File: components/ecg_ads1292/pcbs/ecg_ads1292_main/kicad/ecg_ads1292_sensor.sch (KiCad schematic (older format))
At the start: 36 parts, among them IC1 ADS1292IPBSR, U1 TPS73033DBVT

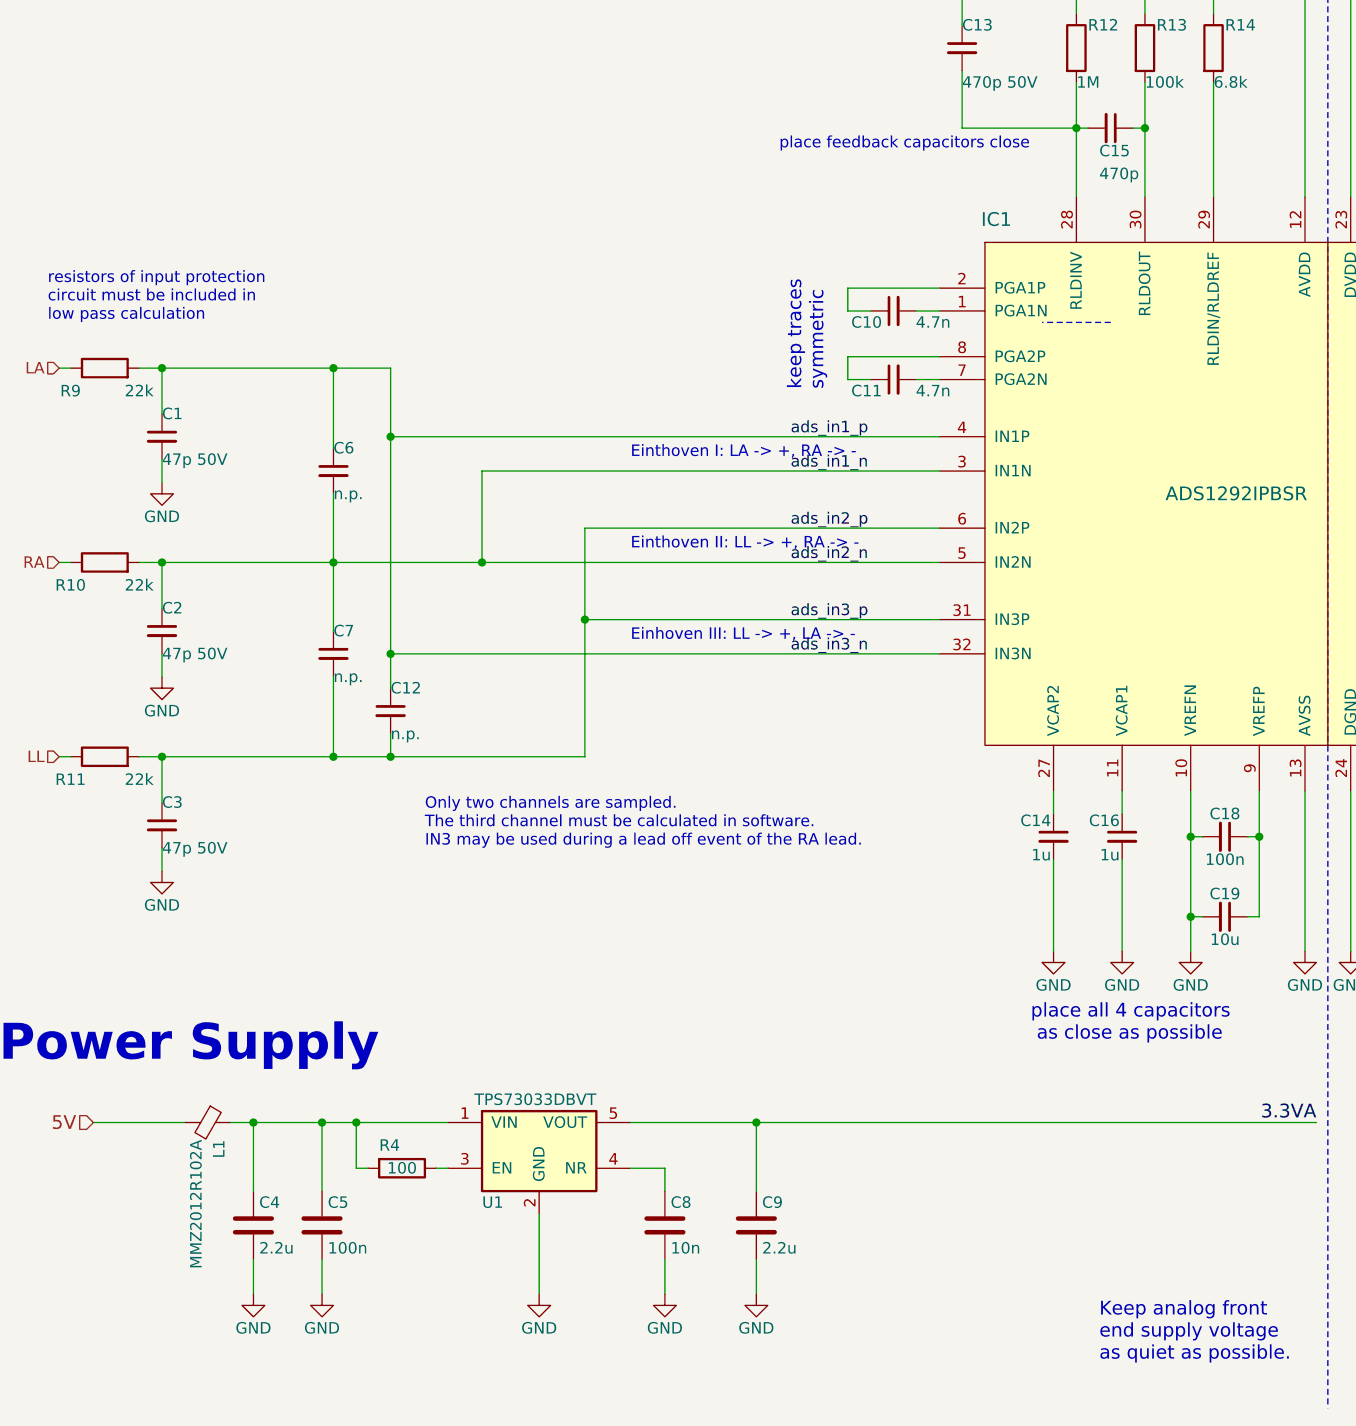
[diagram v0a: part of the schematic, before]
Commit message: update parts and add digikey PNs
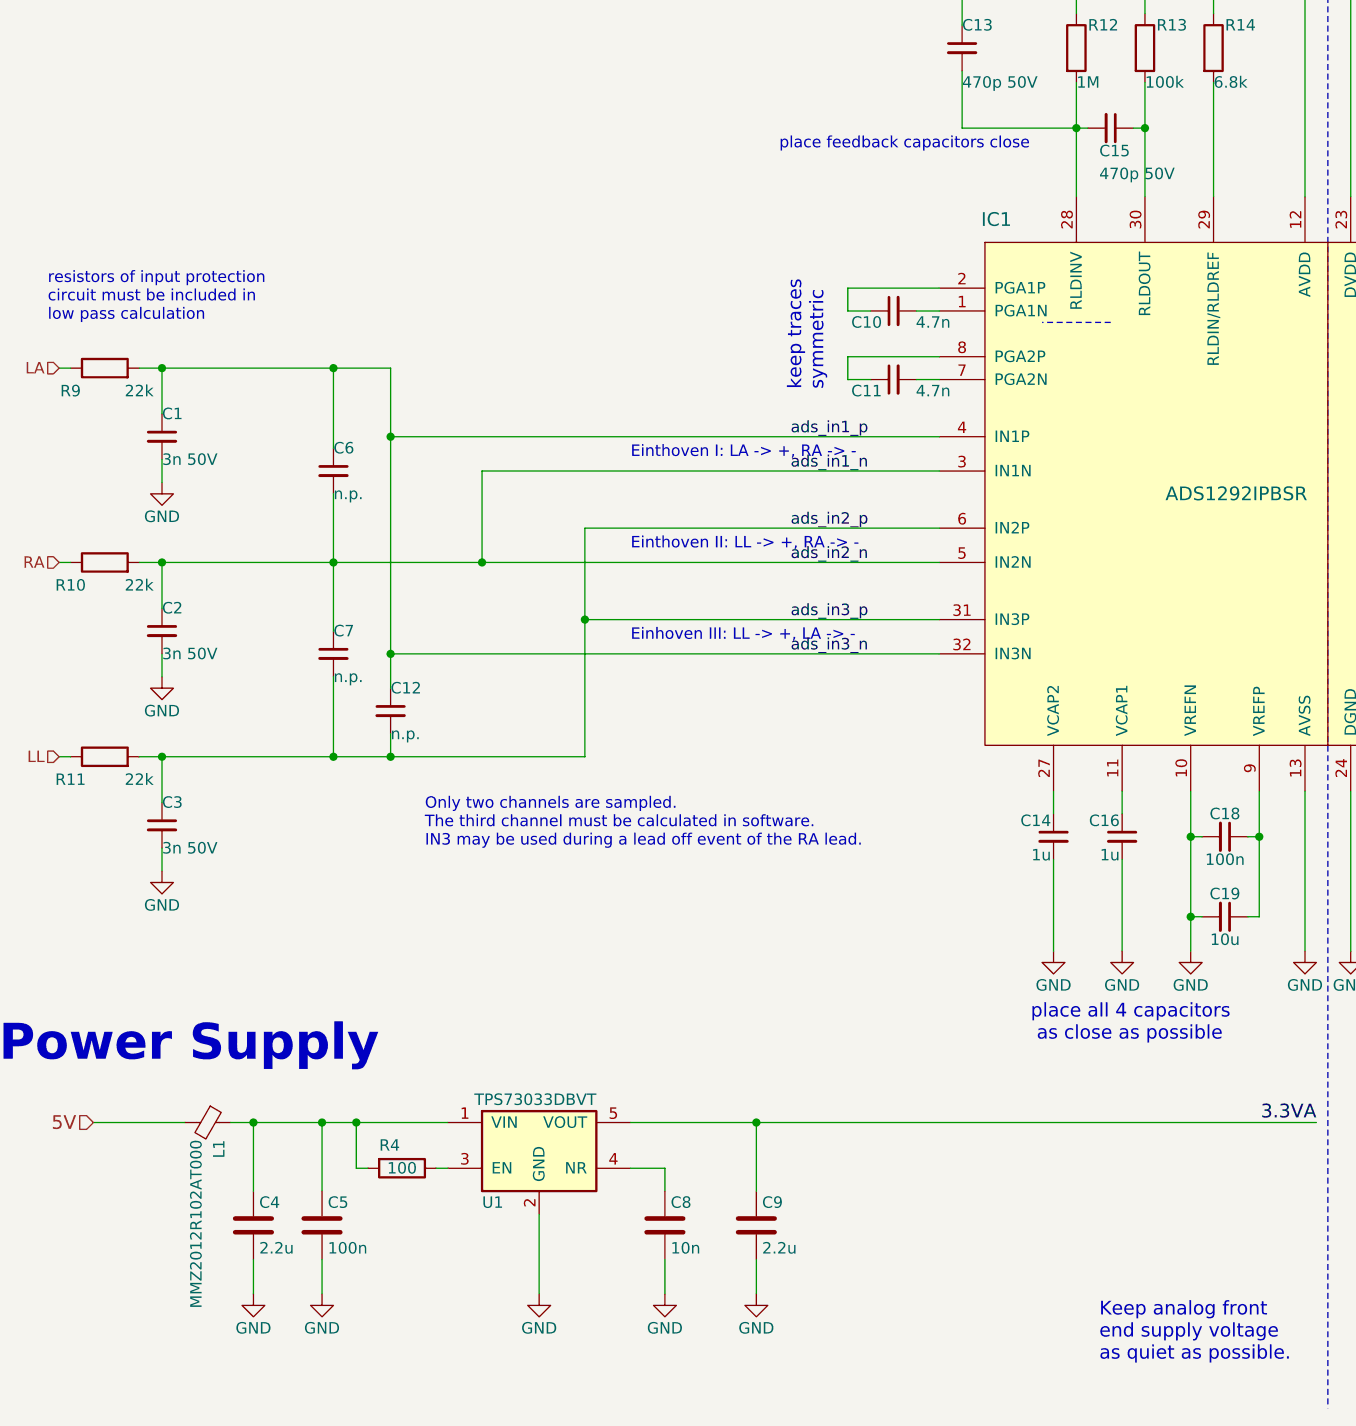
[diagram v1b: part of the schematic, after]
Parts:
- C1, C2, C3: value 47p 50V -> 3n 50V; MPN (none) -> C0603C302J5GAC7867; Manufacturer (none) -> KEMET; PN Digi-Key (none) -> 399-14513-1-ND
- C10, C11: MPN (none) -> GRM1885C1H472JA01D; Manufacturer (none) -> MURATA; PN Digi-Key (none) -> 490-9669-1-ND
- C13: MPN (none) -> C0603C471J5GACTU; Manufacturer (none) -> KEMET; PN Digi-Key (none) -> 399-7922-1-ND; PN Farnell 2627442 -> 1414640
- C14, C16, C21: MPN (none) -> LMK107B7105KA-T; Manufacturer (none) -> TAYO YUDEN; PN Digi-Key (none) -> 587-1242-1-ND
- C15: value 470p -> 470p 50V; MPN (none) -> C0603C471J5GACTU; Manufacturer (none) -> KEMET; PN Digi-Key (none) -> 399-7922-1-ND; PN Farnell 2627442 -> 1414640
- C17, C20, C5: MPN (none) -> C1608X7R1H104K080AA; Manufacturer (none) -> TDK; PN Digi-Key (none) -> 445-1314-1-ND
- C18: MPN (none) -> C1608X7R1H104K080AA; Manufacturer (none) -> TDK; PN Digi-Key (none) -> 445-1314-1-ND; PN Farnell 2494294 -> 1907318
- C19: MPN (none) -> JMK107ABJ106KAHT; Manufacturer (none) -> TAYO YUDEN; PN Digi-Key (none) -> 587-JMK107ABJ106KAHTCT-ND; PN Farnell 1889276 -> 3366802
- C4, C9: MPN (none) -> GRM188R71A225KE15D; Manufacturer (none) -> MURATA; PN Digi-Key (none) -> 490-4520-1-ND
- C6, C7: PN Farnell 1865491 -> (none)
- C8: MPN (none) -> 0603B103K101CT; Manufacturer (none) -> WALSIN; PN Digi-Key (none) -> 1292-1383-1-ND
- IC1: MPN (none) -> ADS1292IPBSR; Manufacturer (none) -> TEXAS INSTRUMENTS; PN Digi-Key (none) -> 296-46284-1-ND
- L1: value MMZ2012R102A -> MMZ2012R102AT000; MPN (none) -> MMZ2012R102AT000; Manufacturer (none) -> TDK; PN Digi-Key (none) -> MMZ2012R102AT000
- R10, R11, R9: MPN (none) -> CRCW060322K0FKEA; Manufacturer (none) -> VISHAY; PN Digi-Key (none) -> 541-4036-1-ND
- R12: MPN (none) -> CRCW06031M00FKEA; Manufacturer (none) -> VISHAY; PN Digi-Key (none) -> 541-1.00MHCT-ND
- R13: MPN (none) -> CRCW0603100KJNEA; Manufacturer (none) -> VISHAY; PN Digi-Key (none) -> 541-100KGCT-ND
- R14, R18, R19: MPN (none) -> CRCW06036K80FKEA; Manufacturer (none) -> VISHAY; PN Digi-Key (none) -> 541-6.80KHCT-ND; PN Farnell 1738916 -> 1469831
- R15, R16, R4: MPN (none) -> CRCW0603100RJNEA; Manufacturer (none) -> VISHAY; PN Digi-Key (none) -> 541-100GCT-ND; PN Farnell 1739145 -> 2616742
- R17: MPN (none) -> CRCW0603100KJNEA; Manufacturer (none) -> VISHAY; PN Digi-Key (none) -> 541-100KGCT-ND; PN Farnell 1739145 -> 1692517
